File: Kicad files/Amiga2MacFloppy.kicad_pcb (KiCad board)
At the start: 2 copper layers, 44 x 48 mm, 12 parts, among them J1 DB23F, J2 Conn_02x10_Odd_Even_MountingP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, J3 DB23M, U1 74LS139, U2 74LS393

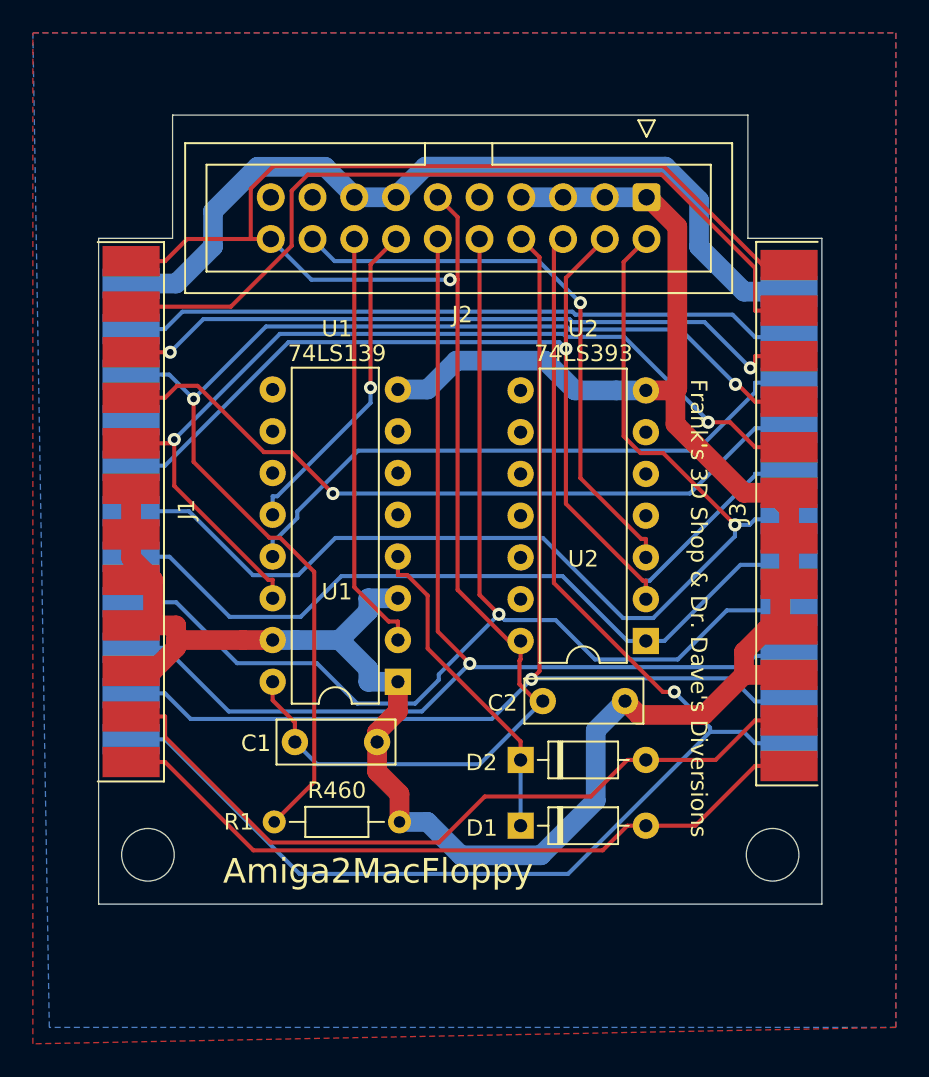
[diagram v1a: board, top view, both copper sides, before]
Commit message: Corrections
Corrected Adapter to Female connector instead of male.
Removed R1
Cleaned up schematics
Added Open Hardware Logo
Cleaned up silkscreens
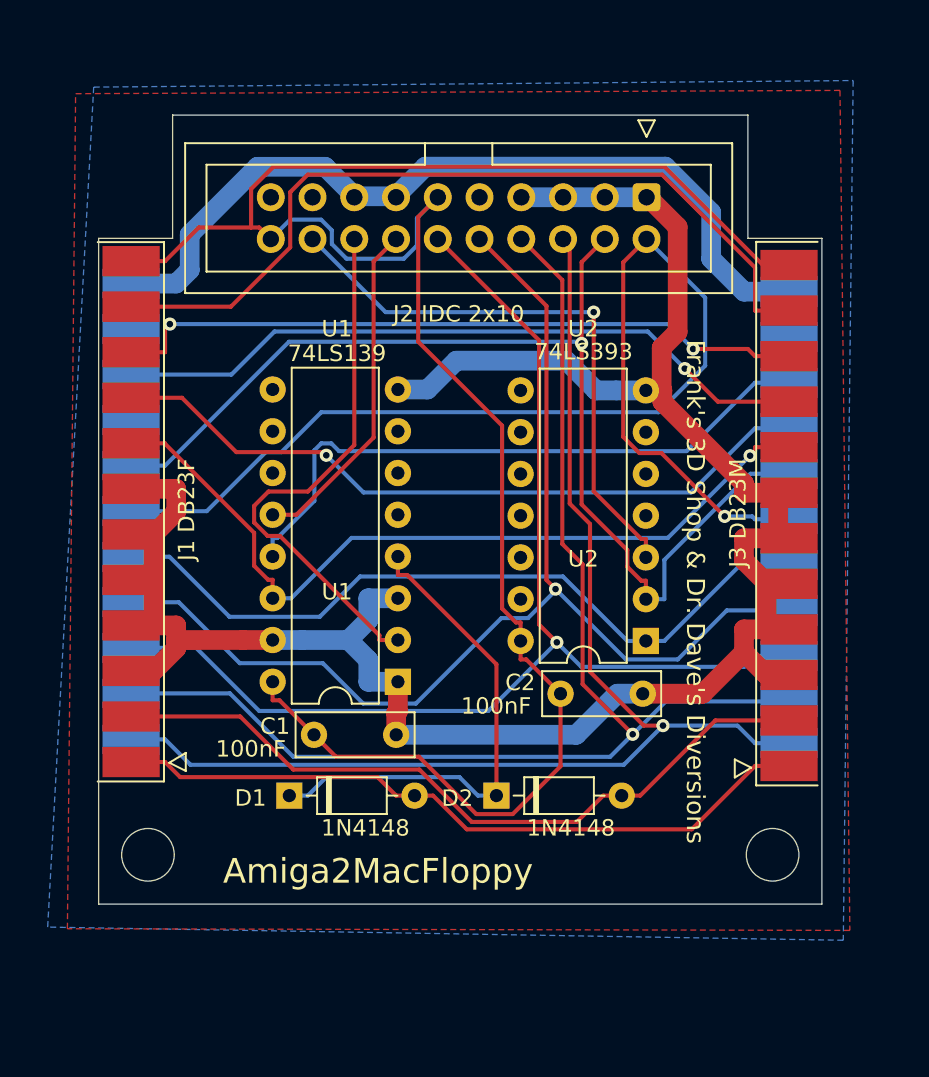
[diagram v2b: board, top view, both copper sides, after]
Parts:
- removed R460: R1, Resistor_THT:R_Axial_DIN0204_L3.6mm_D1.6mm_P7.62mm_Horizontal
- added REF**: OSHW-Logo2_7.3x6mm_SilkScreen, Symbol:OSHW-Logo2_7.3x6mm_SilkScreen, B.Cu at (138.3, 93.2)
- J1: footprint A-Max:DSUB-23_Female_EdgeMount_P2.77mm -> Amiga2MacFloppy:DSUB-23_Female_EdgeMount_P2.77mm
- J3: footprint A-Max:DSUB-23_Male_EdgeMount_P2.77mm -> Amiga2MacFloppy:DSUB-23_Male_EdgeMount_P2.77mm
- moved D1 14.2 mm to (128.1, 122.1)
- moved D2 2.62 mm to (140.7, 122.1)
- moved C1 1.24 mm to (129.6, 118.4)
- moved C2 1.17 mm to (144.6, 115.9)
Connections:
- net PWM renamed +5V
- J1 pad 20: Net-(J1-Pad20) -> (no net)
- J1 pad 22: _INDEX -> (no net)
- J2 pad 17: Net-(J2-Pad17) -> (no net)
- J2 pad 19: Net-(J2-Pad19) -> (no net)
- J2 pad 9: Net-(J2-Pad9) -> (no net)
- J3 pad 22: _INDEX -> (no net)
- U1 pad 10: Net-(U1-Pad10) -> (no net)
- U1 pad 11: Net-(U1-Pad11) -> (no net)
- U1 pad 5: Net-(U1-Pad5) -> (no net)
- U1 pad 6: Net-(U1-Pad6) -> (no net)
- U1 pad 7: Net-(U1-Pad7) -> (no net)
- U1 pad 9: Net-(U1-Pad9) -> (no net)
- U2 pad 10: Net-(U2-Pad10) -> (no net)
- U2 pad 11: Net-(U2-Pad11) -> (no net)
- U2 pad 12: Net-(U2-Pad12) -> (no net)
- U2 pad 13: Net-(U2-Pad13) -> (no net)
- U2 pad 4: Net-(U2-Pad4) -> (no net)
- U2 pad 5: Net-(U2-Pad5) -> (no net)
- U2 pad 6: Net-(U2-Pad6) -> (no net)
- U2 pad 8: Net-(U2-Pad8) -> (no net)
- U2 pad 9: Net-(U2-Pad9) -> (no net)
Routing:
- net _INDEX: track 41.1 -> 0.00 mm
- net _SEL2: track 74.5 -> 42.9 mm, vias 2 -> 1
- net Net-(D1-Pad1): track 19.8 -> 30.9 mm
- net _MTRXD: track 57.9 -> 49.7 mm, vias 2 -> 1
- net +5V: track 116.0 -> 124.2 mm, vias 1 -> 0
- net RD: track 25.8 -> 33.0 mm
- net PH2: track 81.8 -> 74.9 mm
- net PH3: track 69.7 -> 76.0 mm
- net GND: track 142.9 -> 138.8 mm
- net PH0: track 69.1 -> 72.6 mm
- net SEL: track 69.8 -> 71.8 mm
- net _DKRD: track 47.0 -> 45.2 mm
- net _SEL1: track 37.0 -> 38.7 mm
- net _RDY: track 44.4 -> 43.3 mm
- net _DKWE: track 70.7 -> 71.7 mm
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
